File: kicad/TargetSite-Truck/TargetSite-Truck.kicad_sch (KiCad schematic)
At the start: 11 parts, among them J2 HC05, M1 Motor_DC, U1 PIC16F1827-E/P, U2 TA7291P

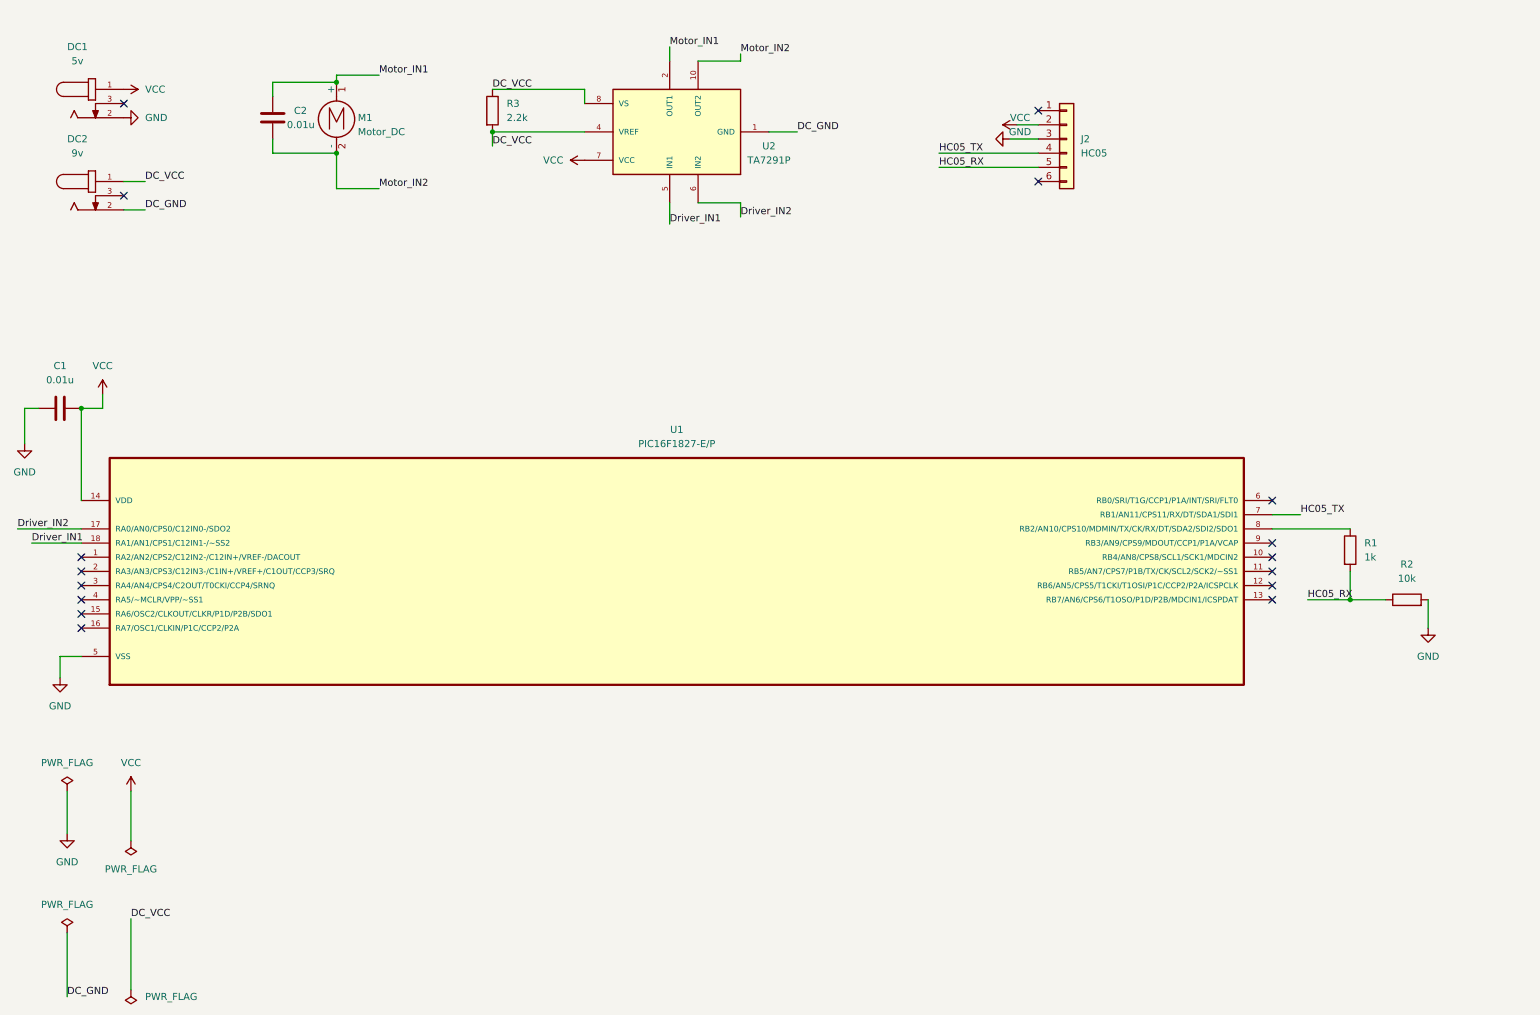
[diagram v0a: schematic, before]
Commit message: 回路図の作成、PCBの作成
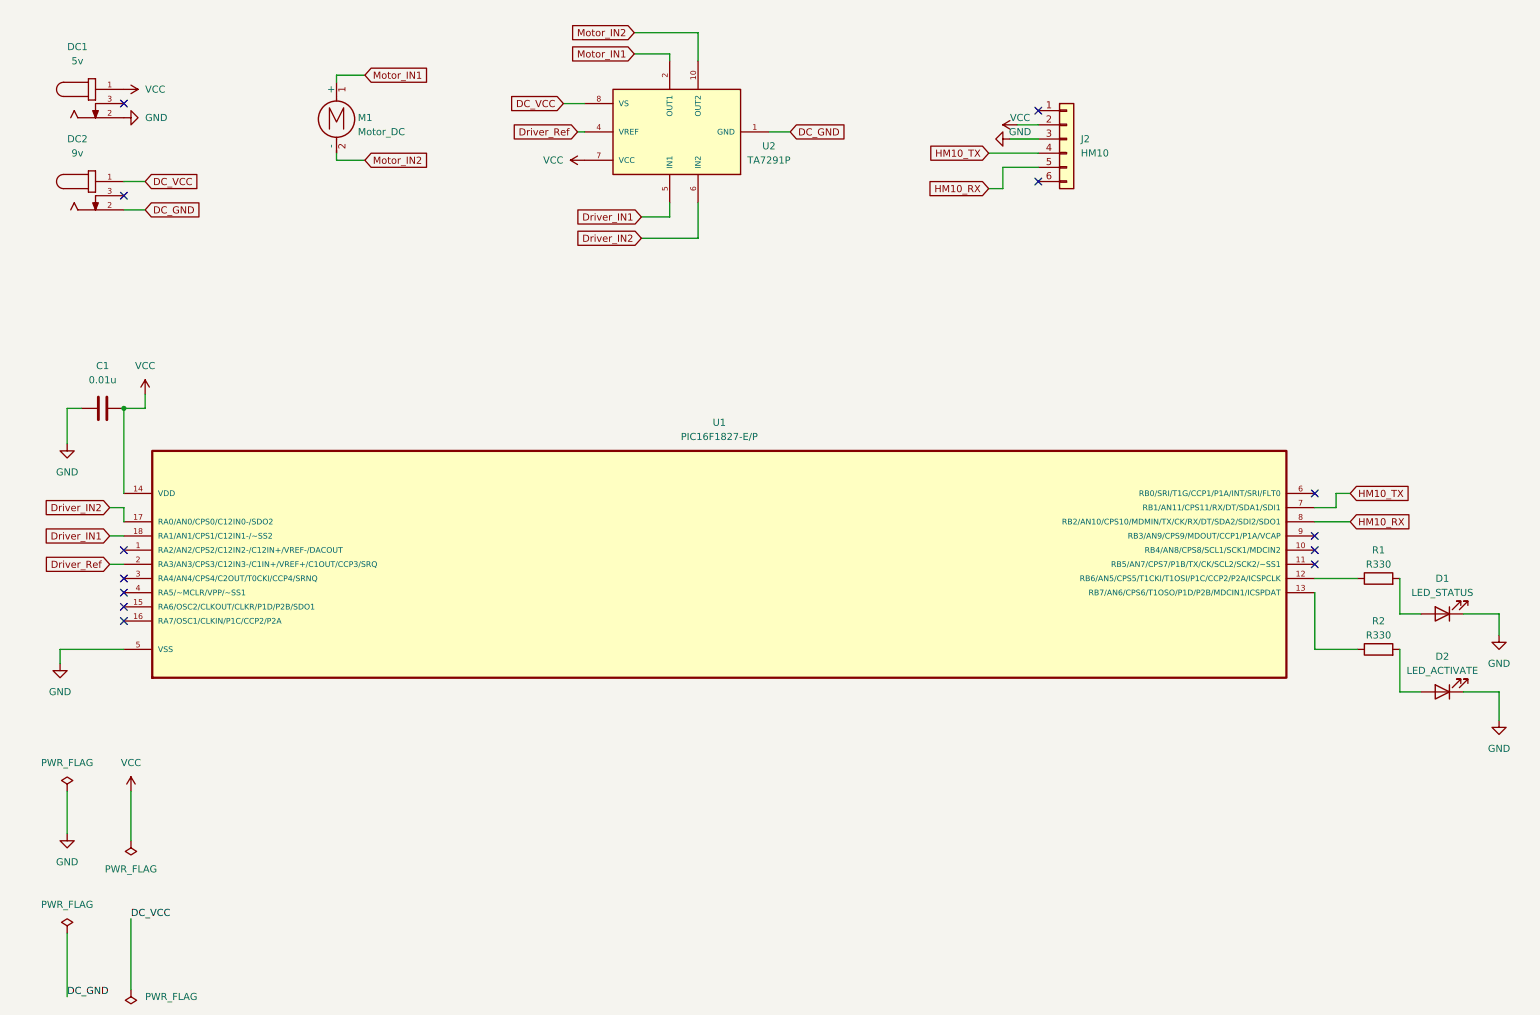
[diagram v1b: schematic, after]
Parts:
- removed C2: 0.01u, Capacitor_THT:C_Disc_D3.0mm_W1.6mm_P2.50mm, symbol Device:C
- removed R3: 2.2k, Resistor_THT:R_Axial_DIN0204_L3.6mm_D1.6mm_P5.08mm_Horizontal, symbol Device:R
- added D1: LED_STATUS, LED_THT:LED_D3.0mm, symbol Device:LED
- added D2: LED_ACTIVATE, LED_THT:LED_D3.0mm, symbol Device:LED
- J2: value HC05 -> HM10
- R1: value 1k -> R330; footprint Resistor_THT:R_Axial_DIN0204_L3.6mm_D1.6mm_P5.08mm_Horizontal -> Resistor_THT:R_Axial_DIN0207_L6.3mm_D2.5mm_P2.54mm_Vertical
- R2: value 10k -> R330; footprint Resistor_THT:R_Axial_DIN0204_L3.6mm_D1.6mm_P5.08mm_Horizontal -> Resistor_THT:R_Axial_DIN0207_L6.3mm_D2.5mm_P2.54mm_Vertical
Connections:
- net DC_VCC: no longer U2.4 (VREF)
- net GND: now also D1.1 (K), D2.1 (K); no longer R2.2
- net at R1.1: now also U1.12 (RB6/AN5/CPS5/T1CKI/T1OSI/P1C/CCP2/P2A/ICSPCLK); no longer U1.8 (RB2/AN10/CPS10/MDMIN/TX/CK/RX/DT/SDA2/SDI2/SDO1)
- net at U1.13 (RB7/AN6/CPS6/T1OSO/P1D/P2B/MDCIN1/ICSPDAT): now also R2.1
- net Driver_Ref: now reaches U1.2 (RA3/AN3/CPS3/C12IN3-/C1IN+/VREF+/C1OUT/CCP3/SRQ)
- net Driver_Ref: now also U2.4 (VREF)
- removed net HC05_RX: J2.5 (Pin_5), R1.2, R2.1
- net HC05_TX renamed HM10_TX
- new net: D2.2 (A), R2.2
- new net: D1.2 (A), R1.2
- new net HM10_RX: J2.5 (Pin_5), U1.8 (RB2/AN10/CPS10/MDMIN/TX/CK/RX/DT/SDA2/SDI2/SDO1)
- no-connect marks 16 -> 13
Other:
- moved on the sheet: C1, U1

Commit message: 回路基板設計修正
RA0、RA1の配線を引き直した
ターミナルのピッチサイズを5.08mmに変更
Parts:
- M1: footprint TerminalBlock_4Ucon:TerminalBlock_4Ucon_1x02_P3.50mm_Horizontal -> TerminalBlock_MetzConnect:TerminalBlock_MetzConnect_Type073_RT02602HBLU_1x02_P5.08mm_Horizontal
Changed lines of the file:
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@@
       (effects (font (size 1.27 1.27)) (justify left))
     )
-    (property "Footprint" "TerminalBlock_4Ucon:TerminalBlock_4Ucon_1x02_P3.50mm_Horizontal" (id 2) (at 72.39 36.576 0)
+    (property "Footprint" "TerminalBlock_MetzConnect:TerminalBlock_MetzConnect_Type073_RT02602HBLU_1x02_P5.08mm_Horizontal" (id 2) (at 72.39 36.576 0)
       (effects (font (size 1.27 1.27)) hide)
     )
@@
     )
     (path "/3839f658-e961-4379-aca0-577d55fa1a30"
-      (reference "M1") (unit 1) (value "Motor_DC") (footprint "TerminalBlock_4Ucon:TerminalBlock_4Ucon_1x02_P3.50mm_Horizontal")
+      (reference "M1") (unit 1) (value "Motor_DC") (footprint "TerminalBlock_MetzConnect:TerminalBlock_MetzConnect_Type073_RT02602HBLU_1x02_P5.08mm_Horizontal")
     )
     (path "/edf7ea70-fb34-43d6-8502-d59a0f625635"

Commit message: Update TargetSite-Truck.kicad_sch
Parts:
- removed D1: LED_STATUS, LED_THT:LED_D3.0mm, symbol Device:LED
- removed D2: LED_ACTIVATE, LED_THT:LED_D3.0mm, symbol Device:LED
- removed DC1: 5v, PJ-002AH:CUI_PJ-002AH, symbol PJ-002AH:PJ-002AH
- removed DC2: 9v, PJ-002AH:CUI_PJ-002AH, symbol PJ-002AH:PJ-002AH
- removed M1: Motor_DC, TerminalBlock_MetzConnect:TerminalBlock_MetzConnect_Type073_RT02602HBLU_1x02_P5.08mm_Horizontal, symbol Motor:Motor_DC
- removed R1, R2: R330, Resistor_THT:R_Axial_DIN0207_L6.3mm_D2.5mm_P2.54mm_Vertical, symbol Device:R
- removed U2: TA7291P, TA7291P:HSIP10, symbol TA7291P:TA7291P
- added D?: LED_STATUS, LED_THT:LED_D3.0mm, symbol Device:LED
- added D?: LED_ACTIVATE, LED_THT:LED_D3.0mm, symbol Device:LED
- added J?: R_IN, symbol Connector_Generic:Conn_01x02
- added J?: FW_IN, symbol Connector_Generic:Conn_01x02
- added J?: L_IN, symbol Connector_Generic:Conn_01x02
- added J?: BK_IN, symbol Connector_Generic:Conn_01x02
- added J?: PIC_WRITER_CON, symbol Connector_Generic:Conn_01x06
- added Q? (x4): 2SC1815, Package_TO_SOT_THT:TO-92_Inline, symbol Transistor_BJT:2SC1815
- added R? (x4): 10K, symbol Device:R
- added R? (x2): R330, Resistor_THT:R_Axial_DIN0207_L6.3mm_D2.5mm_P2.54mm_Vertical, symbol Device:R
- added R?: 10k, Resistor_THT:R_Axial_DIN0207_L6.3mm_D2.5mm_P2.54mm_Vertical, symbol Device:R
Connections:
- net GND: now also D?.1 (K), D?.1 (K), J?.3 (Pin_3), Q?.1 (E), Q?.1 (E), Q?.1 (E), Q?.1 (E)
- net VCC: now also J?.1 (Pin_1), J?.1 (Pin_1), J?.1 (Pin_1), J?.1 (Pin_1), J?.2 (Pin_2), R?.1
- net ICSPDAT_IN: now reaches U1.13 (RB7/AN6/CPS6/T1OSO/P1D/P2B/MDCIN1/ICSPDAT)
- net ISCPCLK_IN: now reaches U1.12 (RB6/AN5/CPS5/T1CKI/T1OSI/P1C/CCP2/P2A/ICSPCLK)
- net R_IN: now reaches U1.1 (RA2/AN2/CPS2/C12IN2-/C12IN+/VREF-/DACOUT)
- net R_IN: now also R?.1
- net LED_ACTIVATE_IN: now reaches U1.10 (RB4/AN8/CPS8/SCL1/SCK1/MDCIN2)
- net LED_ACTIVATE_IN: now also R?.1
- net at U1.4 (RA5/~MCLR/VPP/~SS1): now also R?.2
- net LED_STATUS_IN: now reaches U1.9 (RB3/AN9/CPS9/MDOUT/CCP1/P1A/VCAP)
- net LED_STATUS_IN: now also R?.1
- net Driver_IN1 renamed BK_IN
- net BK_IN: now also R?.1
- net Driver_IN2 renamed FW_IN
- net FW_IN: now also R?.1
- net Driver_Ref renamed L_IN
- net L_IN: now also R?.1
- new net: J?.2 (Pin_2), Q?.2 (C) (x4)
- new net: Q?.3 (B), R?.2 (x4)
- new net: D?.2 (A), R?.2 (x2)
- new net ISCPDAT_IN: J?.4 (Pin_4)
- new net ISCP_CLK_IN: J?.5 (Pin_5)
- no-connect marks 13 -> 7
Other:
- moved on the sheet: C1, J2, U1
